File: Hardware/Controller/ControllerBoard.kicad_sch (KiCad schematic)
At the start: 30 parts, among them J1 Conn_01x08_MountingPin, J2 USB_C_Receptacle_USB2.0, J4 Interface, J5 I2C, J6 I2C ThroughHole, U1 ESP32-S3-WROOM-1, U2 SN65220, U3 TLV62569DBV

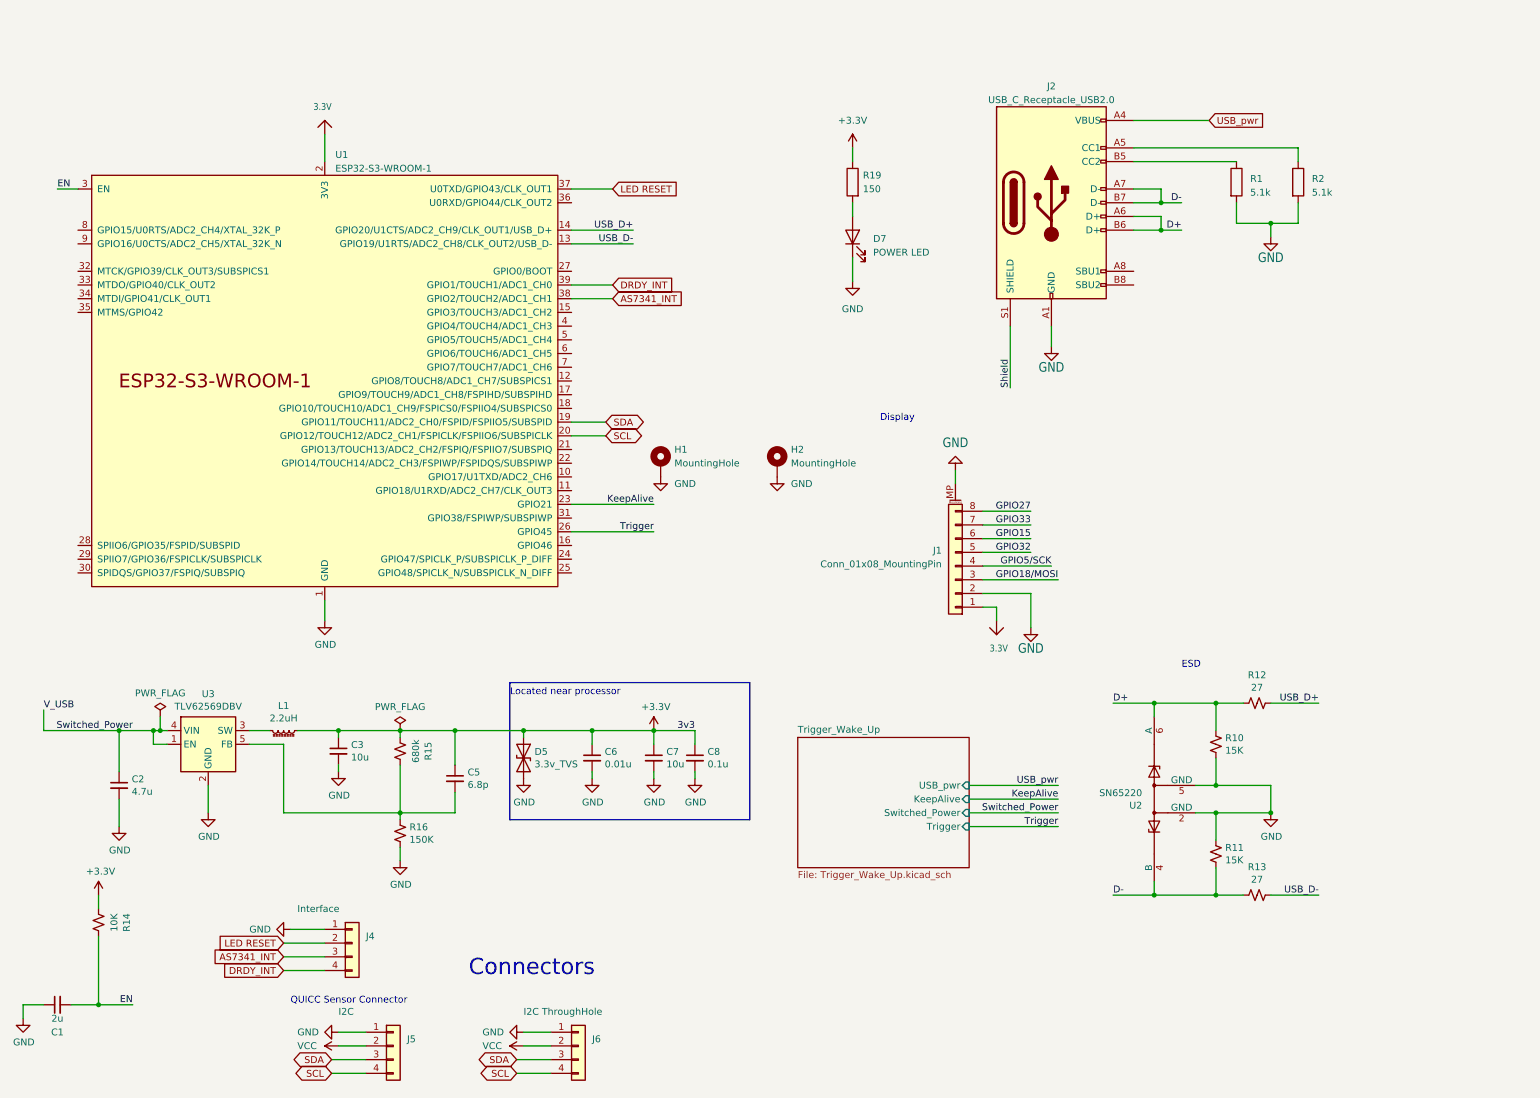
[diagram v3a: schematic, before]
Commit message: updated routing on control board, added led pcb template
Signed-off-by: lokimetasmith <lokimail@gmail.com>
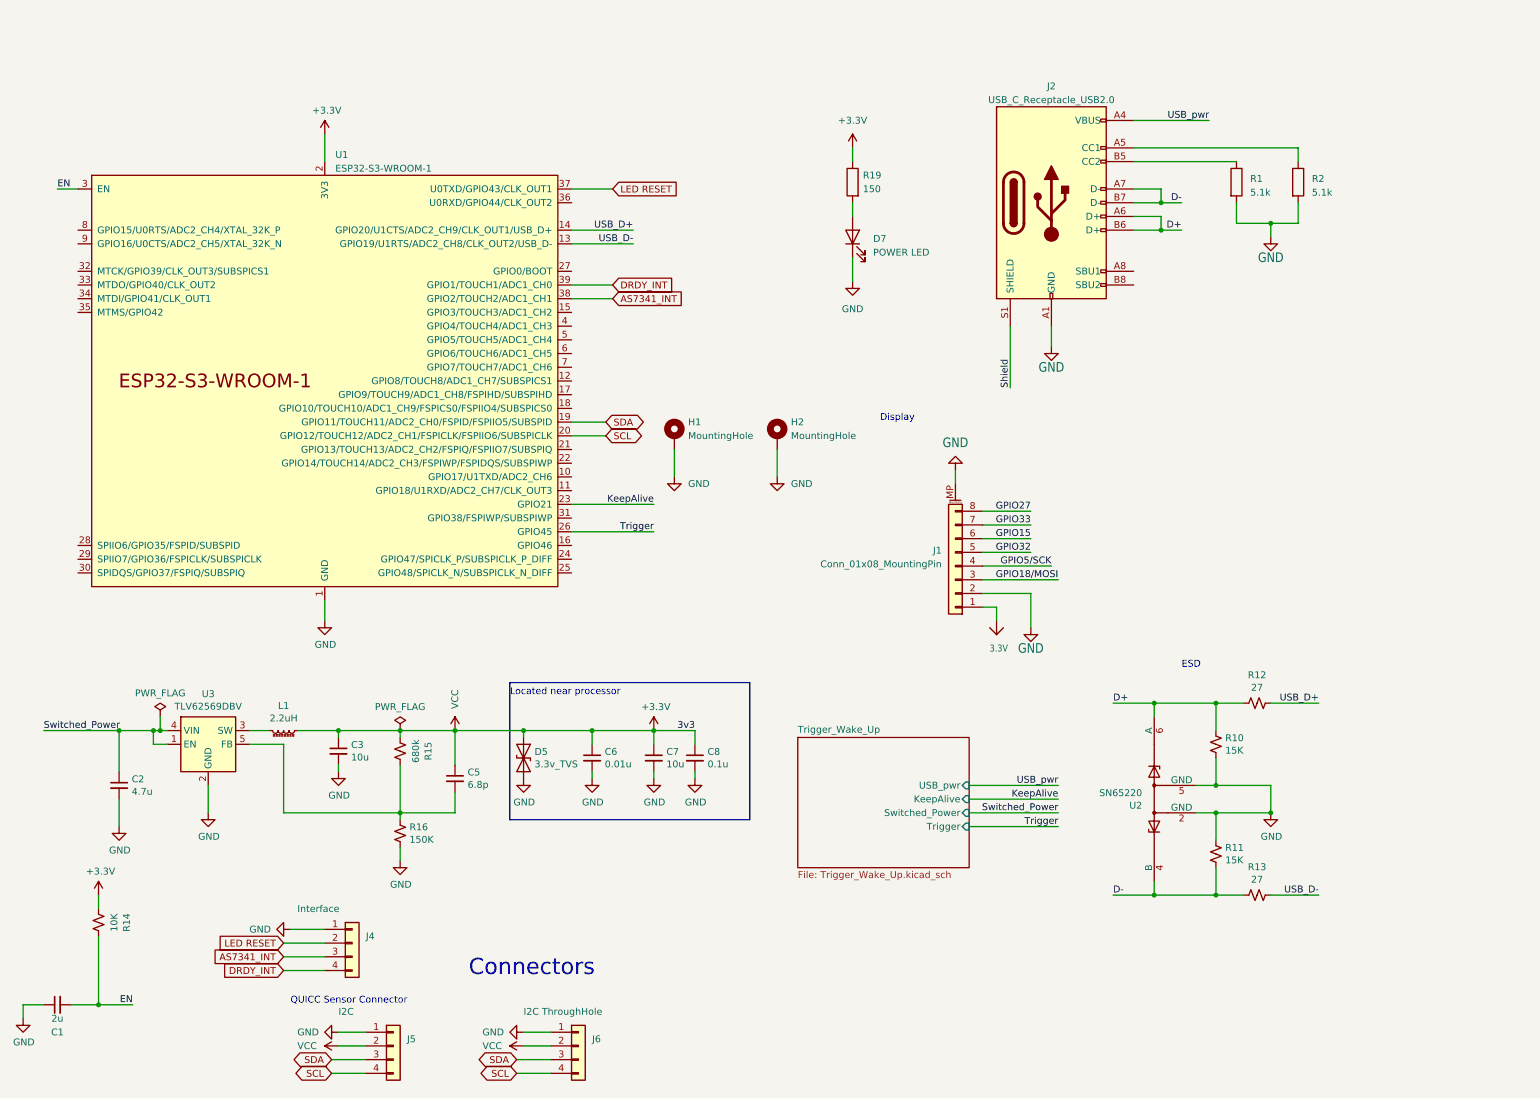
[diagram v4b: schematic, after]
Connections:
- net VCC is gone; now on net +3V3: J5.2 (Pin_2), J6.2 (Pin_2)
- net +3V3: now also U1.2 (3V3)
- net 3.3V: no longer U1.2 (3V3)
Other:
- moved on the sheet: H1, H2
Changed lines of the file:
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@@
+    (stroke (width 0) (type default))
+  )
+  (wire (pts (xy 139.7 82.55) (xy 139.7 87.63))
     (stroke (width 0) (type default))
   )
@@
     (stroke (width 0) (type default))
   )
+  (wire (pts (xy 158.75 82.55) (xy 158.75 87.63))
+    (stroke (width 0) (type default))
+  )
   (wire (pts (xy 194.31 144.78) (xy 210.82 144.78))
     (stroke (width 0) (type default))
@@
   )
   (wire (pts (xy 196.85 99.06) (xy 205.74 99.06))
-    (stroke (width 0) (type default))
-  )
-  (wire (pts (xy 22.86 130.81) (xy 22.86 134.62))
     (stroke (width 0) (type default))
   )
@@
   )
   (label "D+" (at 220.98 129.54 0) (fields_autoplaced)
-    (effects (font (size 1.27 1.27)) (justify left bottom))
-  )
-  (label "V_USB" (at 22.86 130.81 0) (fields_autoplaced)
     (effects (font (size 1.27 1.27)) (justify left bottom))
   )
@@
     (effects (font (size 1.27 1.27)) (justify right bottom))
   )
-  (label "Switched_Power" (at 39.37 134.62 180) (fields_autoplaced)
-    (effects (font (size 1.27 1.27)) (justify right bottom))
+  (label "Switched_Power" (at 22.86 134.62 0) (fields_autoplaced)
+    (effects (font (size 1.27 1.27)) (justify left bottom))
   )
   (label "D-" (at 233.68 36.83 180) (fields_autoplaced)
@@
     )
   )
+  (label "USB_pwr" (at 238.76 21.59 180) (fields_autoplaced)
+    (effects (font (size 1.27 1.27)) (justify right bottom))
+    (property "Intersheetrefs" "${INTERSHEET_REFS}" (at 229.8751 21.59 0)
+      (effects (font (size 1.27 1.27)) (justify right) hide)
+    )
+  )
   (label "USB_D-" (at 259.08 165.1 180) (fields_autoplaced)
     (effects (font (size 1.27 1.27)) (justify right bottom))
@@
     (property "Intersheetrefs" "${INTERSHEET_REFS}" (at 104.5693 198.0406 0)
       (effects (font (size 1.27 1.27)) (justify right) hide)
-    )
-  )
-  (global_label "USB_pwr" (shape input) (at 238.76 21.59 0) (fields_autoplaced)
-    (effects (font (size 1.27 1.27)) (justify left))
-    (property "Intersheetrefs" "${INTERSHEET_REFS}" (at 249.2164 21.5106 0)
-      (effects (font (size 1.27 1.27)) (justify left) hide)
     )
   )
@@
     )
   )
-  (symbol (lib_id "power:GND") (at 137.16 87.63 0) (unit 1)
+  (symbol (lib_id "power:GND") (at 139.7 87.63 0) (unit 1)
     (in_bom yes) (on_board yes) (dnp no) (fields_autoplaced)
-    (property "Reference" "#PWR024" (at 137.16 93.98 0)
-      (effects (font (size 1.27 1.27)) hide)
-    )
-    (property "Value" "GND" (at 139.7 88.8999 0)
-      (effects (font (size 1.27 1.27)) (justify left))
-    )
-    (property "Footprint" "" (at 137.16 87.63 0)
-      (effects (font (size 1.27 1.27)) hide)
-    )
-    (property "Datasheet" "" (at 137.16 87.63 0)
+    (property "Reference" "#PWR024" (at 139.7 93.98 0)
+      (effects (font (size 1.27 1.27)) hide)
+    )
+    (property "Value" "GND" (at 142.24 88.8999 0)
+      (effects (font (size 1.27 1.27)) (justify left))
+    )
+    (property "Footprint" "" (at 139.7 87.63 0)
+      (effects (font (size 1.27 1.27)) hide)
+    )
+    (property "Datasheet" "" (at 139.7 87.63 0)
       (effects (font (size 1.27 1.27)) hide)
     )
@@
     )
   )
-  (symbol (lib_id "ControllerBoard-eagle-import:3.3V") (at 74.93 21.59 0) (unit 1)
-    (in_bom yes) (on_board yes) (dnp no)
-    (property "Reference" "#U0102" (at 74.93 21.59 0)
-      (effects (font (size 1.27 1.27)) hide)
-    )
-    (property "Value" "3.3V" (at 76.2 19.05 0)
-      (effects (font (size 1.27 1.0795)) (justify right))
-    )
-    (property "Footprint" "ControllerBoard:" (at 74.93 21.59 0)
-      (effects (font (size 1.27 1.27)) hide)
-    )
-    (property "Datasheet" "" (at 74.93 21.59 0)
-      (effects (font (size 1.27 1.27)) hide)
-    )
-    (pin "1")
-    (instances
-      (project "ControllerBoard"
-        (path "/87b8a818-7e02-4010-87ed-f48f8c369cfd"
-          (reference "#U0102") (unit 1)
-        )
-      )
-    )
-  )
   (symbol (lib_id "temp-sensor-rescue:GND-power-temp-sensor-rescue") (at 36.83 152.4 0) (unit 1)
     (in_bom yes) (on_board yes) (dnp no)
@@
     )
   )
-  (symbol (lib_id "Mechanical:MountingHole_Pad") (at 158.75 85.09 0) (unit 1)
+  (symbol (lib_id "Mechanical:MountingHole_Pad") (at 158.75 80.01 0) (unit 1)
     (in_bom no) (on_board yes) (dnp no) (fields_autoplaced)
-    (property "Reference" "H2" (at 161.29 82.5499 0)
-      (effects (font (size 1.27 1.27)) (justify left))
-    )
-    (property "Value" "MountingHole" (at 161.29 85.0899 0)
-      (effects (font (size 1.27 1.27)) (justify left))
-    )
-    (property "Footprint" "MountingHole:MountingHole_2.2mm_M2_ISO7380_Pad" (at 158.75 85.09 0)
-      (effects (font (size 1.27 1.27)) hide)
-    )
-    (property "Datasheet" "~" (at 158.75 85.09 0)
+    (property "Reference" "H2" (at 161.29 77.4699 0)
+      (effects (font (size 1.27 1.27)) (justify left))
+    )
+    (property "Value" "MountingHole" (at 161.29 80.0099 0)
+      (effects (font (size 1.27 1.27)) (justify left))
+    )
+    (property "Footprint" "MountingHole:MountingHole_2.2mm_M2_ISO7380_Pad" (at 158.75 80.01 0)
+      (effects (font (size 1.27 1.27)) hide)
+    )
+    (property "Datasheet" "~" (at 158.75 80.01 0)
       (effects (font (size 1.27 1.27)) hide)
     )
@@
     )
   )
-  (symbol (lib_id "Mechanical:MountingHole_Pad") (at 137.16 85.09 0) (unit 1)
+  (symbol (lib_id "Mechanical:MountingHole_Pad") (at 139.7 80.01 0) (unit 1)
     (in_bom no) (on_board yes) (dnp no) (fields_autoplaced)
-    (property "Reference" "H1" (at 139.7 82.5499 0)
-      (effects (font (size 1.27 1.27)) (justify left))
-    )
-    (property "Value" "MountingHole" (at 139.7 85.0899 0)
-      (effects (font (size 1.27 1.27)) (justify left))
-    )
-    (property "Footprint" "MountingHole:MountingHole_2.2mm_M2_ISO7380_Pad" (at 137.16 85.09 0)
-      (effects (font (size 1.27 1.27)) hide)
-    )
-    (property "Datasheet" "~" (at 137.16 85.09 0)
+    (property "Reference" "H1" (at 142.24 77.4699 0)
+      (effects (font (size 1.27 1.27)) (justify left))
+    )
+    (property "Value" "MountingHole" (at 142.24 80.0099 0)
+      (effects (font (size 1.27 1.27)) (justify left))
+    )
+    (property "Footprint" "MountingHole:MountingHole_2.2mm_M2_ISO7380_Pad" (at 139.7 80.01 0)
+      (effects (font (size 1.27 1.27)) hide)
+    )
+    (property "Datasheet" "~" (at 139.7 80.01 0)
       (effects (font (size 1.27 1.27)) hide)
     )
@@
         (path "/87b8a818-7e02-4010-87ed-f48f8c369cfd"
           (reference "H1") (unit 1)
+        )
+      )
+    )
+  )
+  (symbol (lib_id "temp-sensor-rescue:+3.3V-power-temp-sensor-rescue") (at 74.93 24.13 0) (unit 1)
+    (in_bom yes) (on_board yes) (dnp no)
+    (property "Reference" "#PWR027" (at 74.93 27.94 0)
+      (effects (font (size 1.27 1.27)) hide)
+    )
+    (property "Value" "+3.3V" (at 75.311 19.7358 0)
+      (effects (font (size 1.27 1.27)))
+    )
+    (property "Footprint" "" (at 74.93 24.13 0)
+      (effects (font (size 1.27 1.27)) hide)
+    )
+    (property "Datasheet" "" (at 74.93 24.13 0)
+      (effects (font (size 1.27 1.27)) hide)
+    )
+    (pin "1")
+    (instances
+      (project "ControllerBoard"
+        (path "/87b8a818-7e02-4010-87ed-f48f8c369cfd"
+          (reference "#PWR027") (unit 1)
+        )
+      )
+      (project "temp sensor"
+        (path "/e0f06b5c-de63-4833-a591-ca9e19217a35"
+          (reference "#PWR04") (unit 1)
         )
       )
@@
         )
       )
+    )
+  )
+  (symbol (lib_id "power:VCC") (at 99.06 134.62 0) (unit 1)
+    (in_bom yes) (on_board yes) (dnp no)
+    (property "Reference" "#PWR026" (at 99.06 138.43 0)
+      (effects (font (size 1.27 1.27)) hide)
+    )
+    (property "Value" "VCC" (at 99.06 127 90)
+      (effects (font (size 1.27 1.27)) (justify right))
+    )
+    (property "Footprint" "" (at 99.06 134.62 0)
+      (effects (font (size 1.27 1.27)) hide)
+    )
+    (property "Datasheet" "" (at 99.06 134.62 0)
+      (effects (font (size 1.27 1.27)) hide)
+    )
+    (pin "1")
+    (instances
+      (project "ControllerBoard"
+        (path "/87b8a818-7e02-4010-87ed-f48f8c369cfd"
+          (reference "#PWR026") (unit 1)
+        )
+      )

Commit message: as ordered 11/27/2023 from JLCPCB
Updated silk on RoundScanner, minor changes,

major changes on control board, cleaned up foot prints, nudged parts around
control board not ready for release yet
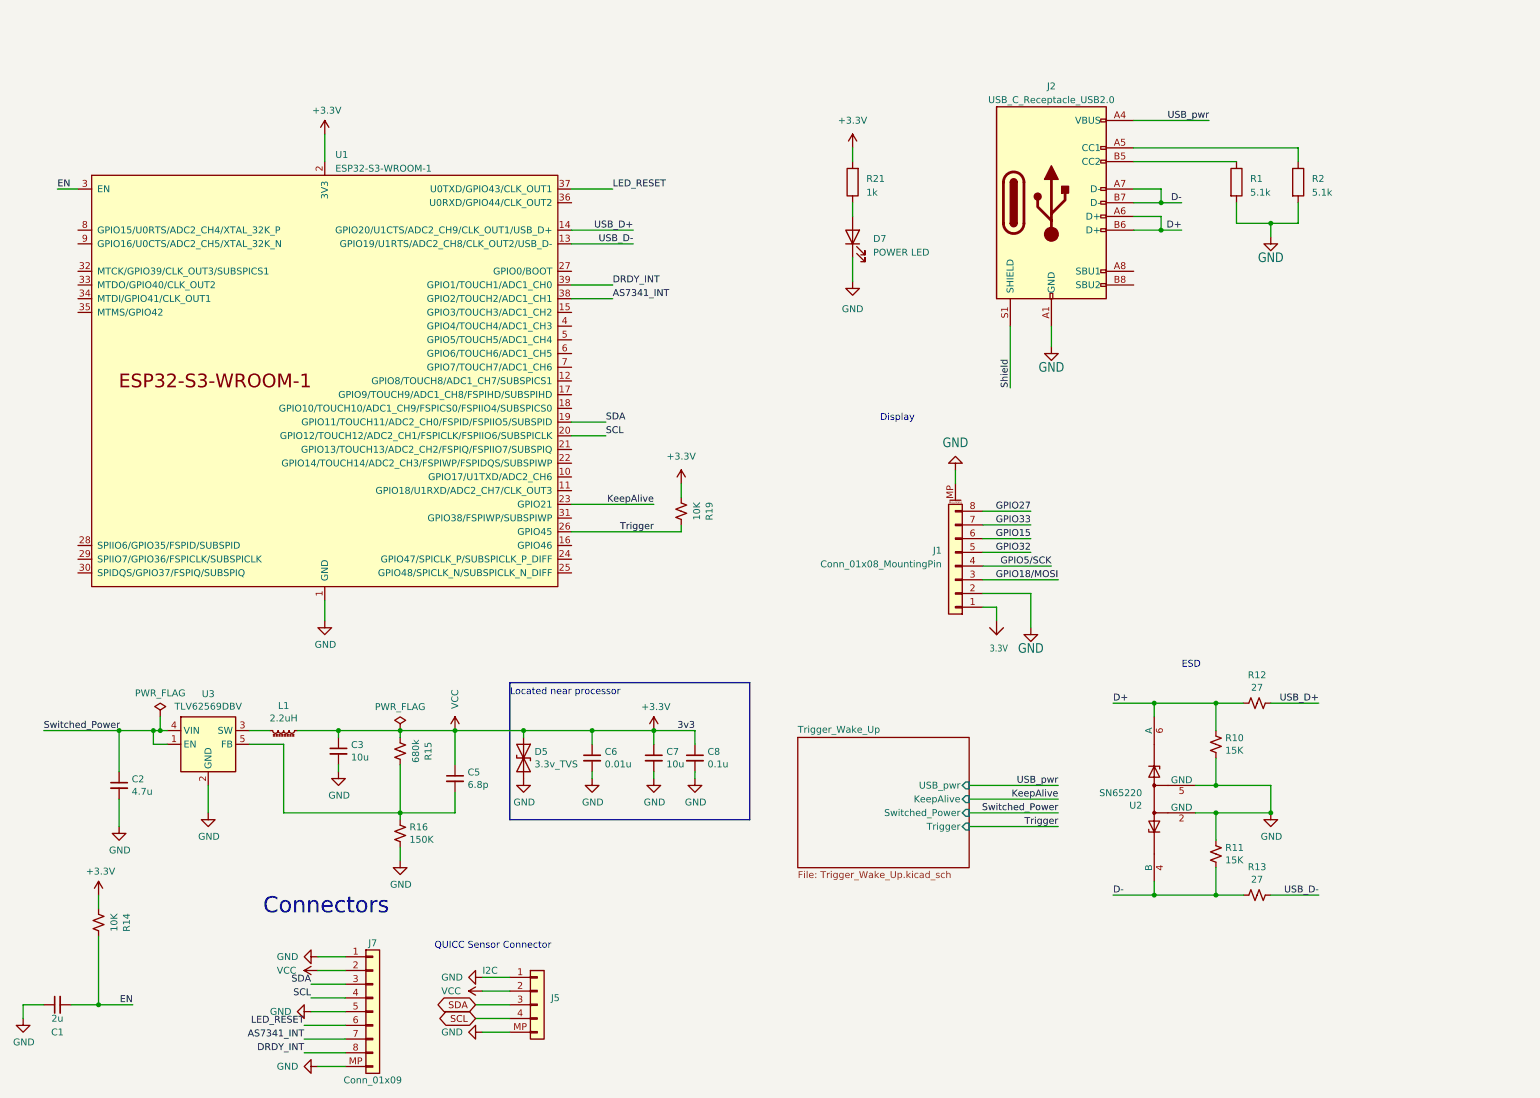
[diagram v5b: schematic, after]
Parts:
- removed H1, H2: MountingHole, MountingHole:MountingHole_2.2mm_M2_ISO7380_Pad, symbol Mechanical:MountingHole_Pad
- removed J4: Interface, Connector_PinSocket_2.54mm:PinSocket_1x04_P2.54mm_Vertical, symbol Connector_Generic:Conn_01x04
- removed J6: I2C ThroughHole, Connector_PinSocket_2.54mm:PinSocket_1x04_P2.54mm_Vertical, symbol Connector_Generic:Conn_01x04
- removed R19: 150, Resistor_SMD:R_0402_1005Metric, symbol Device:R
- added J7: Conn_01x09, round_module:round_notch, symbol Connector_Generic:Conn_01x09
- added R19: 10K, Resistor_SMD:R_0402_1005Metric, symbol temp-sensor-rescue:R_Small_US-Device-temp-sensor-rescue
- added R21: 1k, Resistor_SMD:R_0402_1005Metric, symbol Device:R
- C3, C7: footprint Capacitor_SMD:C_1206_3216Metric_Pad1.42x1.75mm_HandSolder -> Capacitor_SMD:C_1206_3216Metric_Pad1.33x1.80mm_HandSolder
- J5: symbol Connector_Generic:Conn_01x04 -> Connector_Generic:Conn_01x05
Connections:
- net +3V3: now also J7.2 (Pin_2), R19.2, R21.2
- net AS7341_INT: now also J7.7 (Pin_7)
- net DRDY_INT: now also J7.8 (Pin_8)
- net GND: now also J5.MP (Pin_5), J7.1 (Pin_1), J7.5 (Pin_5), J7.MP
- net SCL: now also J7.4 (Pin_4)
- net SDA: now also J7.3 (Pin_3)
- net Trigger: now also R19.1
- net at D7.2 (A): now also R21.1
- net LED RESET renamed LED_RESET
- net LED_RESET: now also J7.6 (Pin_6)
